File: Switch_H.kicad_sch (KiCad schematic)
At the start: 9 parts, among them Q801 NMOS, Q802 NMOS, U801 LM74700, U802 LM74700, U803 TMCS1101A2UQDT

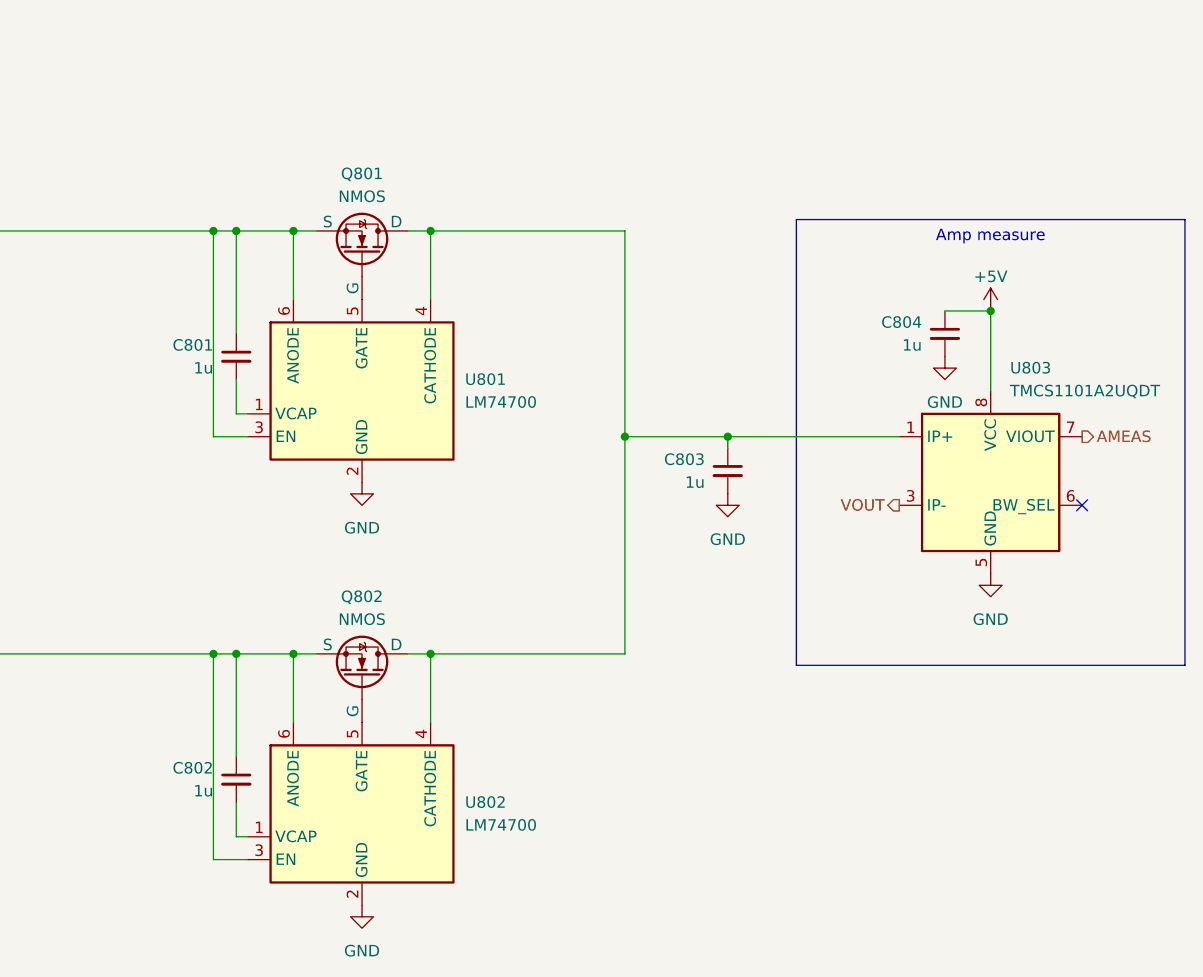
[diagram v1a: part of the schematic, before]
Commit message: updated battery pack module; updated solar inputs module
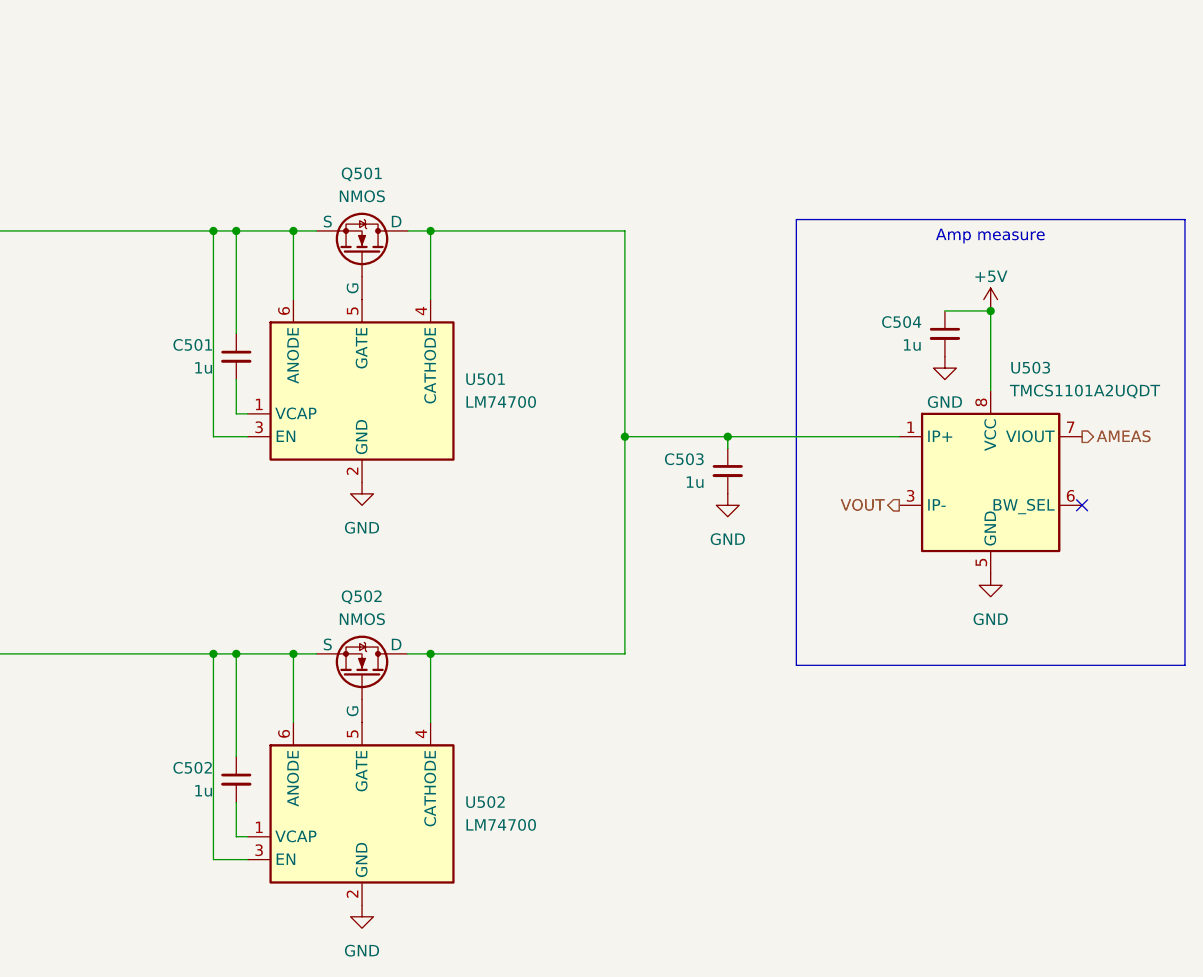
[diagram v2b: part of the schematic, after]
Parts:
- Q501: renamed from Q801; footprint Package_TO_SOT_SMD:SOT-23-6 -> Outlines:NVTFS5116PLTWG
- Q502: renamed from Q802; footprint Package_TO_SOT_SMD:SOT-23-6 -> Outlines:NVTFS5116PLTWG
- renumbered C801 to C501, C802 to C502, C803 to C503, C804 to C504, U801 to U501, U802 to U502, U803 to U503

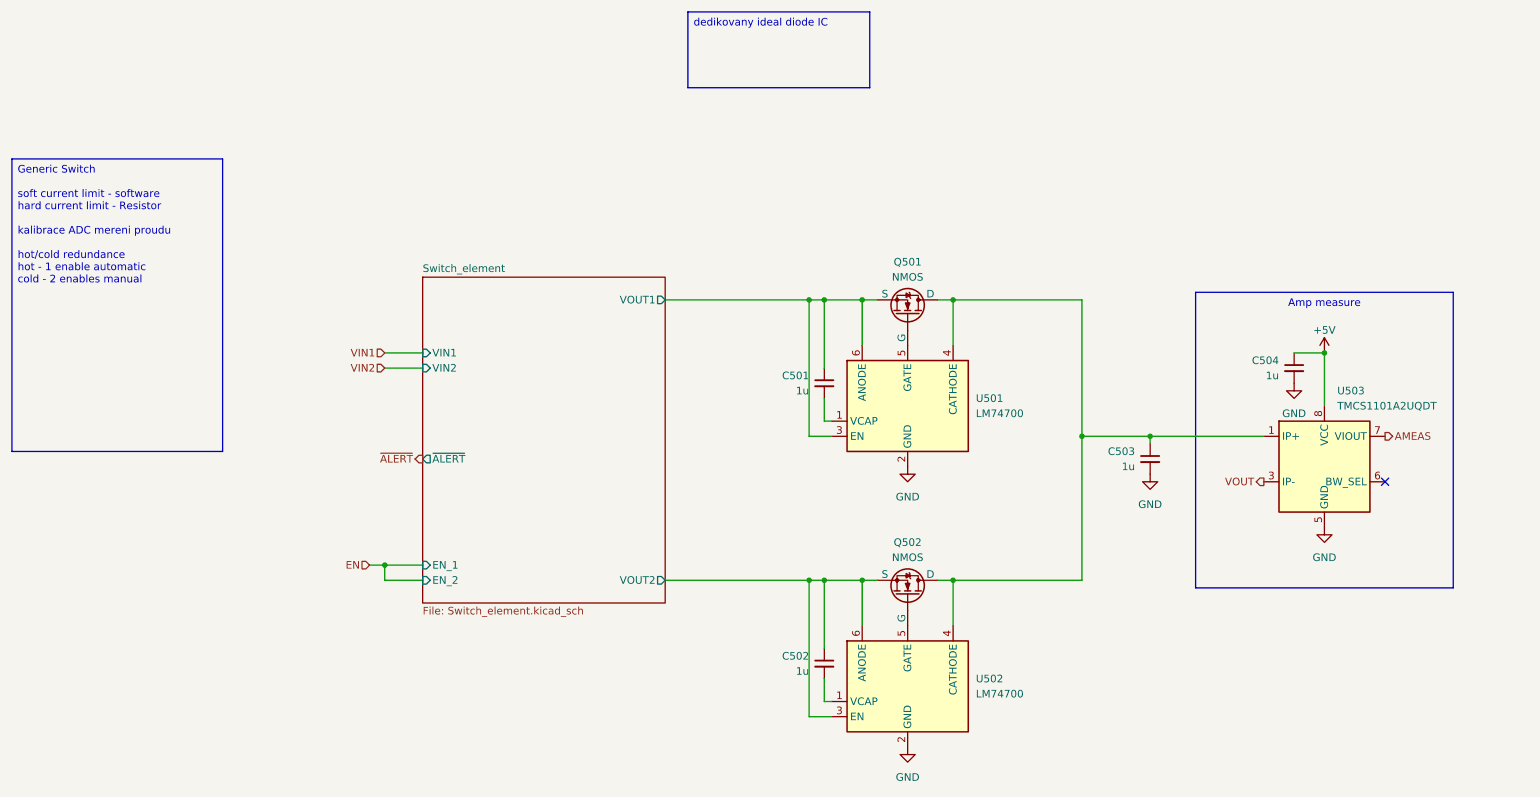
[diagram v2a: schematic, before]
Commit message: added values to most parts
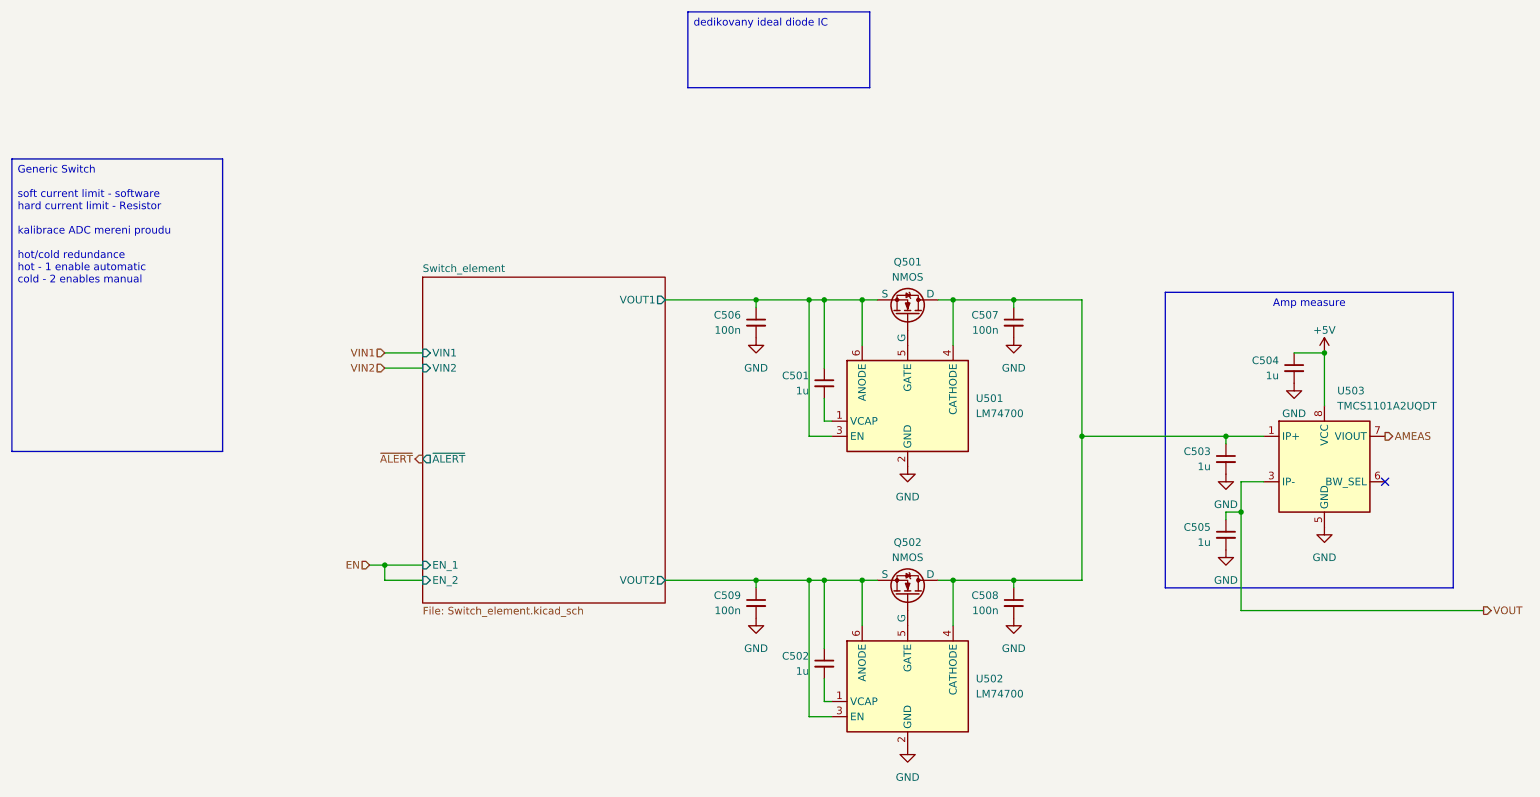
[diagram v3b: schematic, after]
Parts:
- added C505: 1u, Capacitor_SMD:C_0603_1608Metric_Pad1.08x0.95mm_HandSolder, symbol Device:C_Small
- added C506, C507, C508, C509: 100n, Capacitor_SMD:C_0603_1608Metric_Pad1.08x0.95mm_HandSolder, symbol Device:C_Small
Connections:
- net GND: now also C505.2, C506.2, C507.2, C508.2, C509.2
- net Switch_element/VOUT1: now also C506.1
- net Switch_element/VOUT2: now also C509.1
- net VOUT: now also C505.1
- net at C503.1, Q501.1 (D), Q502.1 (D)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: now also C507.1, C508.1
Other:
- moved on the sheet: C503

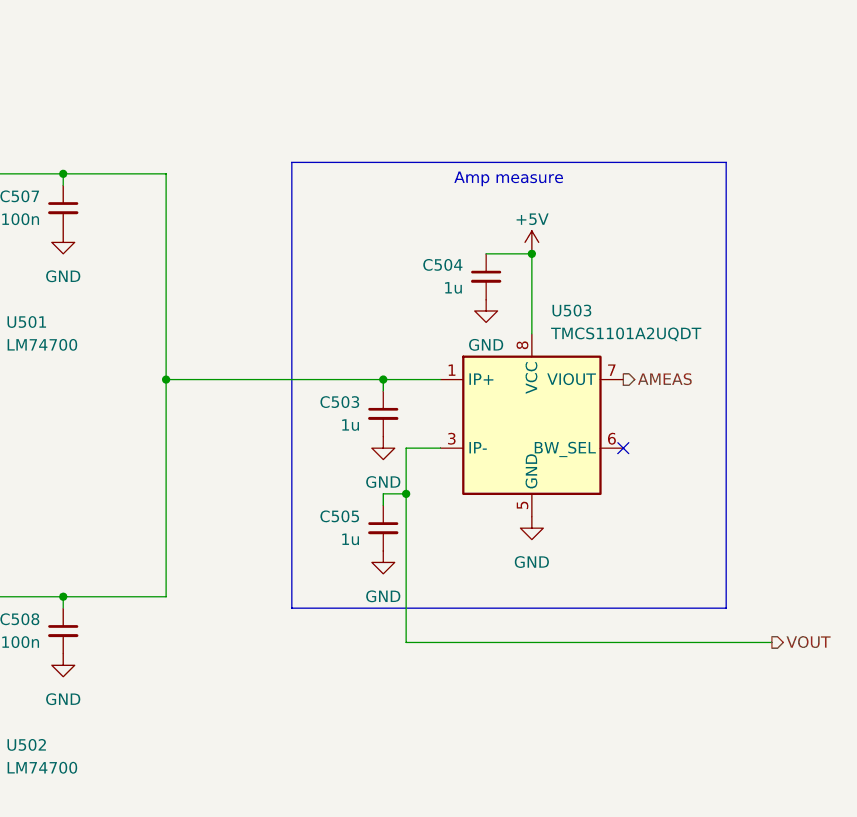
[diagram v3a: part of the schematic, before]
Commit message: deleted unused sheets, added standalone current measure sheet
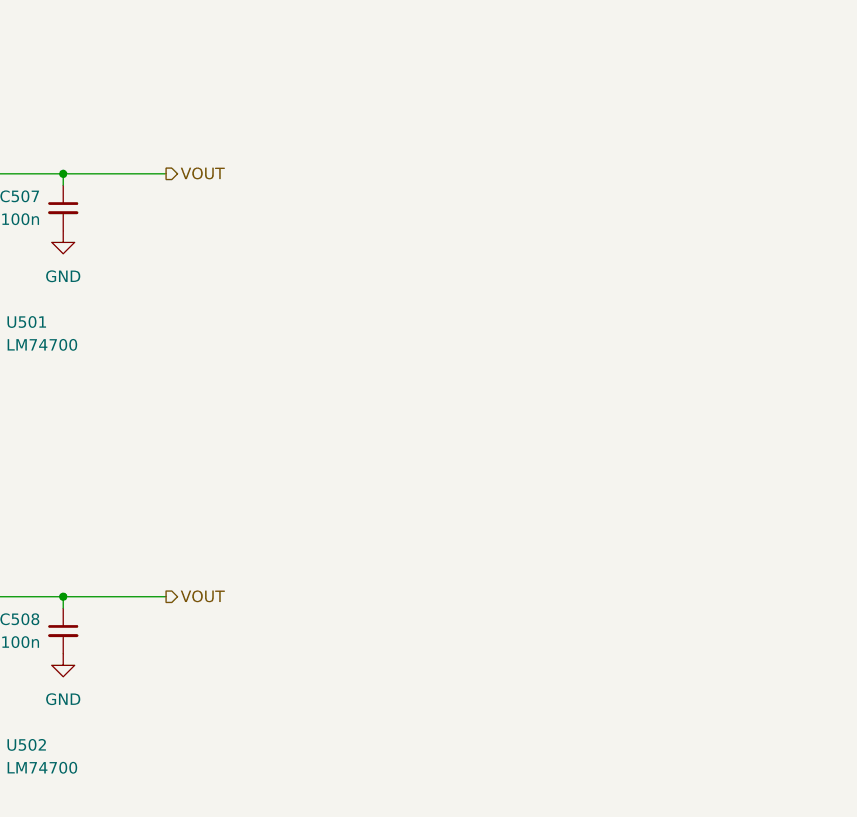
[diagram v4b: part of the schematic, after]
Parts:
- removed C503, C504, C505: 1u, Capacitor_SMD:C_0603_1608Metric_Pad1.08x0.95mm_HandSolder, symbol Device:C_Small
- removed U503: TMCS1101A2UQDT, Package_SO:SOIC-8_3.9x4.9mm_P1.27mm, symbol Sensor_Current:ACS723xLCTR-40AB
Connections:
- net VOUT: now also C507.1, C508.1, Q501.1 (D), Q502.1 (D), U501.4 (CATHODE), U502.4 (CATHODE)
- no-connect marks 1 -> 0

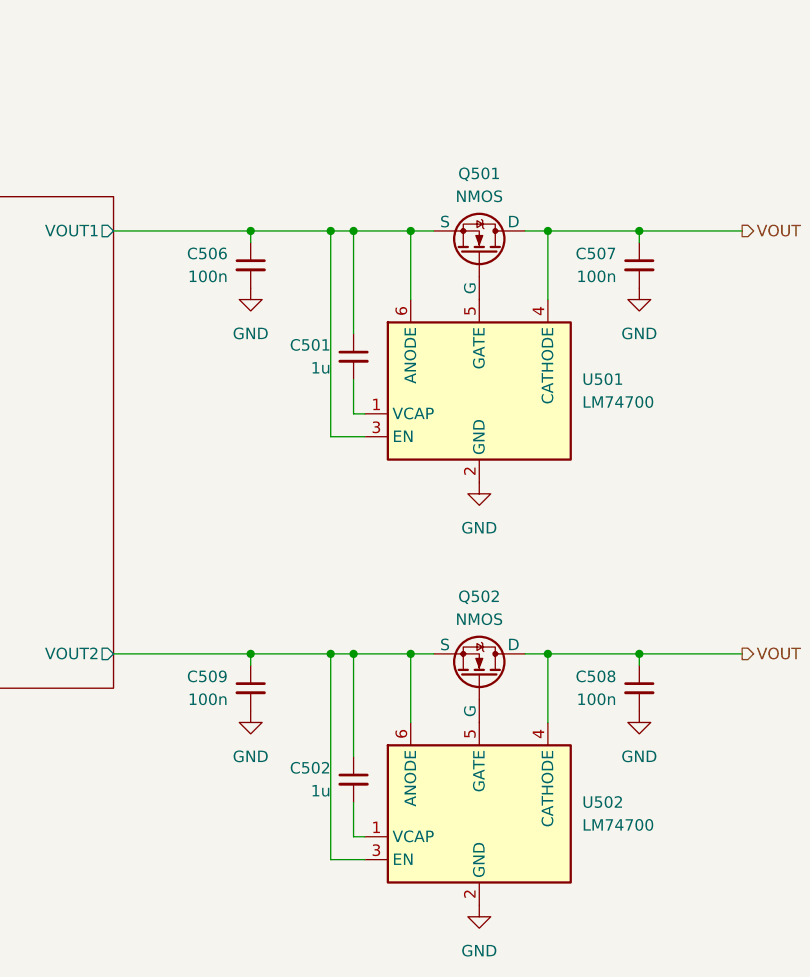
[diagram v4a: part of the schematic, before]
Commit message: wired channel alerts; added schematic for test pbc
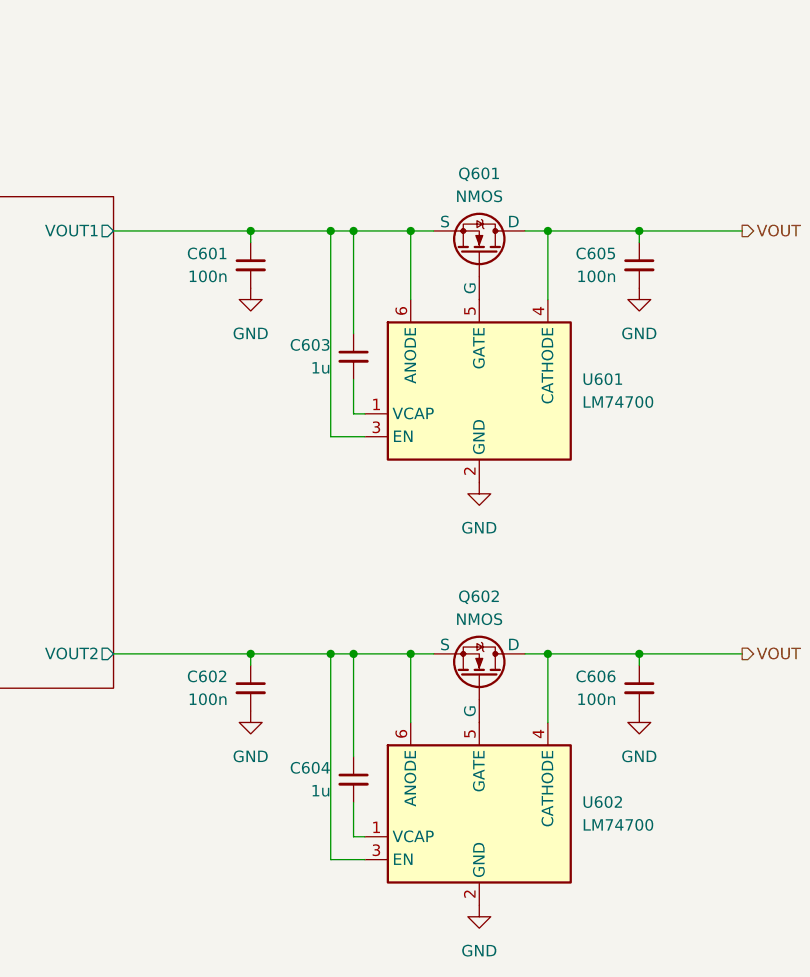
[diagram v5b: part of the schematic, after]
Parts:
- renumbered C506 to C601, C509 to C602, C501 to C603, C502 to C604, C507 to C605, C508 to C606, Q501 to Q601, Q502 to Q602, U501 to U601, U502 to U602

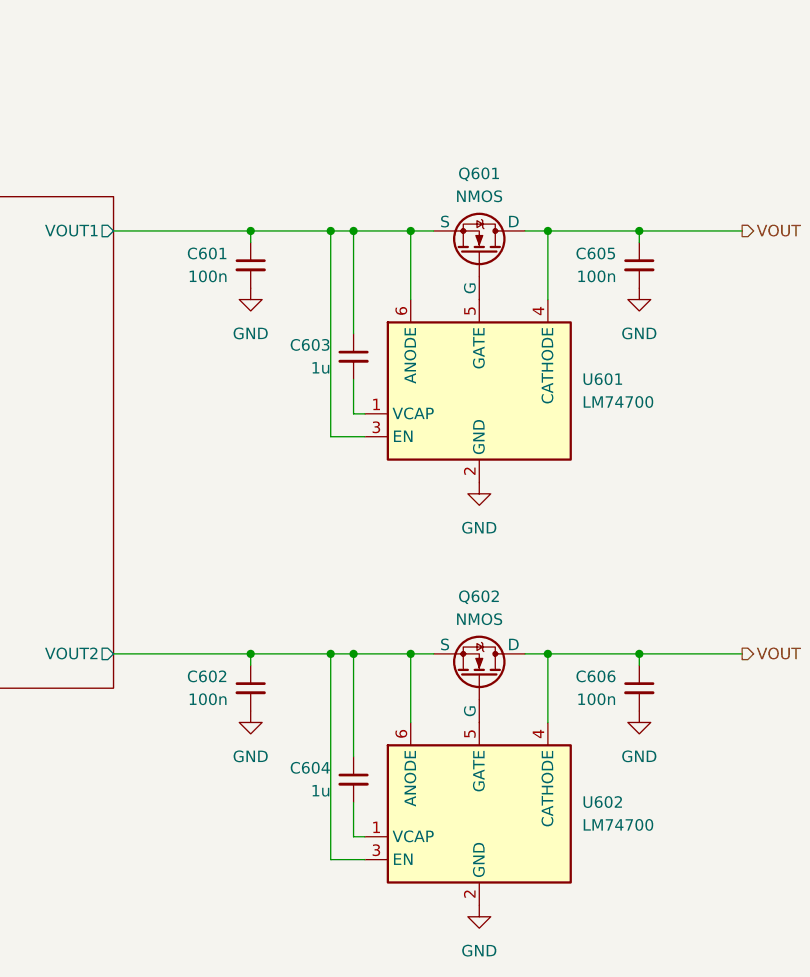
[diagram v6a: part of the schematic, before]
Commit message: added missing heater connectors
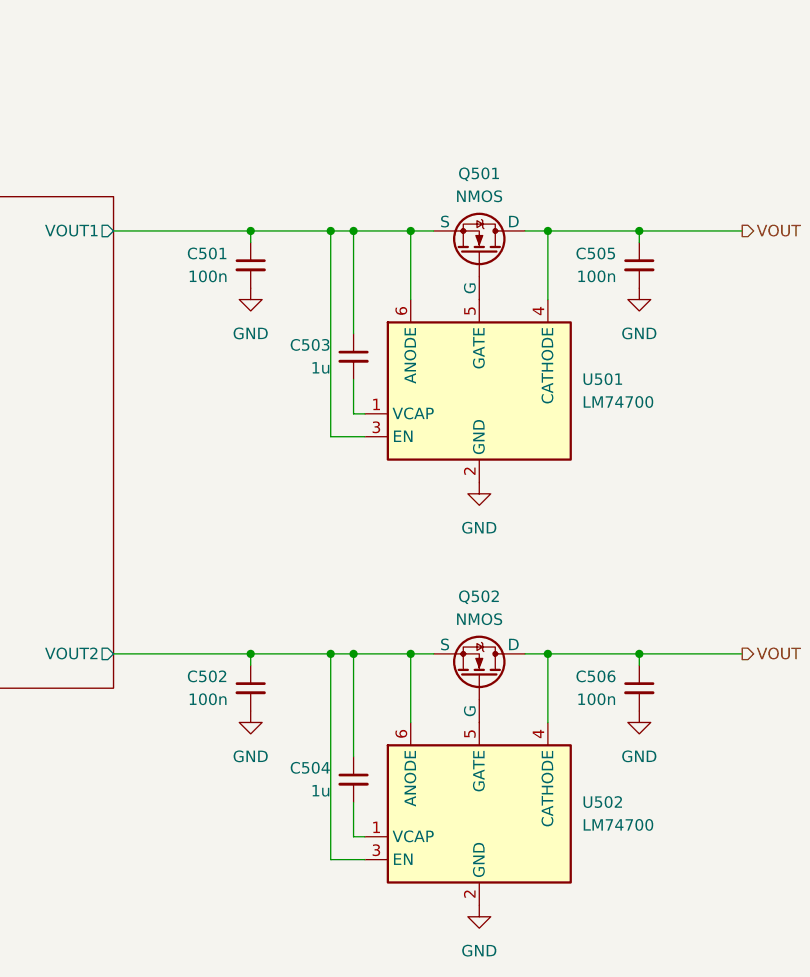
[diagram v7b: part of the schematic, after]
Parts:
- renumbered C601 to C501, C602 to C502, C603 to C503, C604 to C504, C605 to C505, C606 to C506, Q601 to Q501, Q602 to Q502, U601 to U501, U602 to U502
